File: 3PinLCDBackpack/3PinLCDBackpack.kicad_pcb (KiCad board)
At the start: 2 copper layers, 46.4 x 15.2 mm, 7 parts, among them J1 2-pin_power_input_header, J2 3-pin_LCD_header, Q1 BC547, U1 74HC595, U2 LCD_HD44780

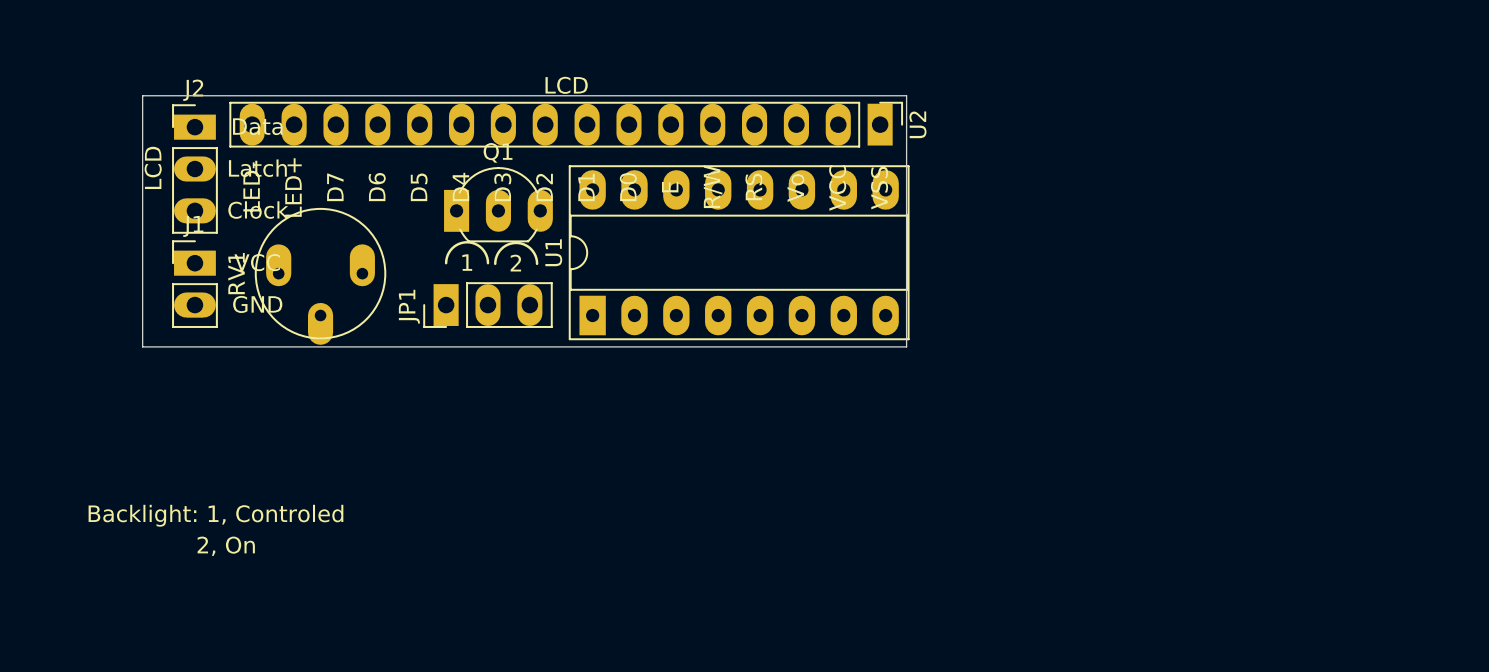
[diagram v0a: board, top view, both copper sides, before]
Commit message: 3 pin lcd backpack, new pcb
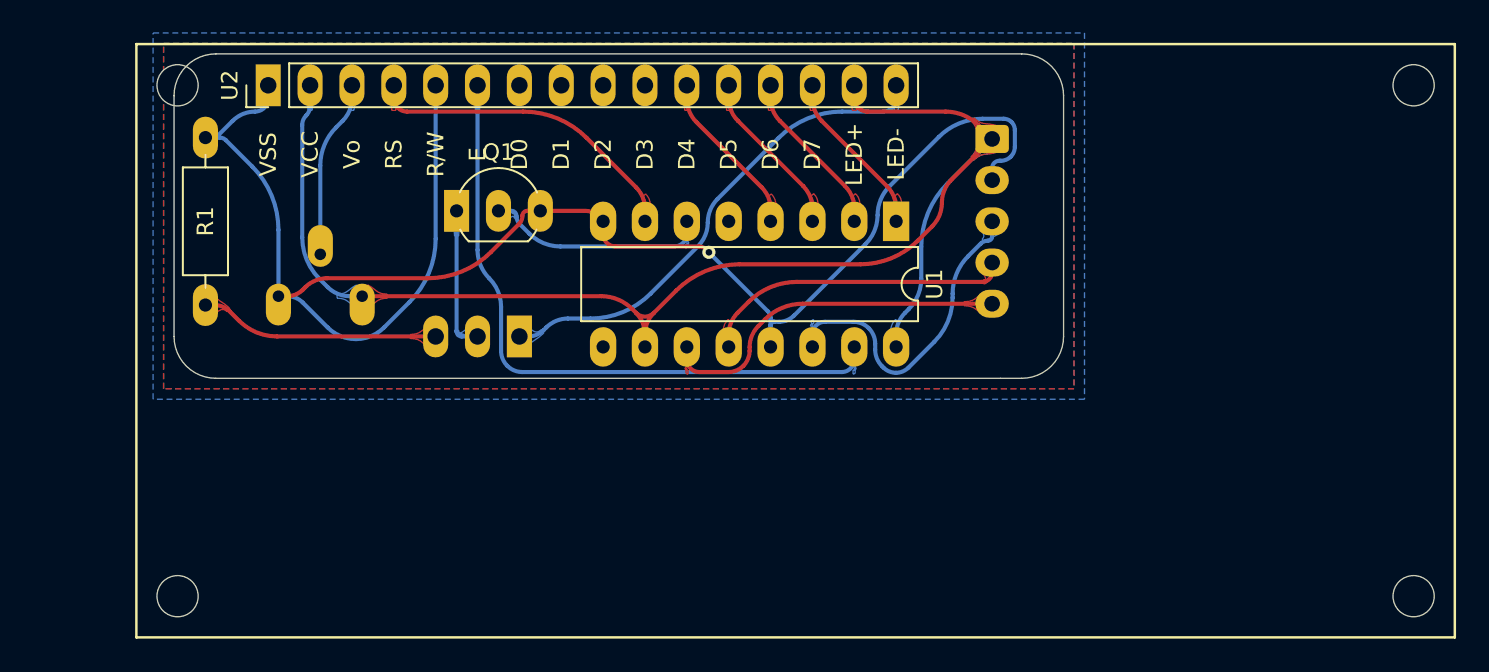
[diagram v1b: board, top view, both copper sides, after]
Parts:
- removed J1: 2-pin_power_input_header, My_Headers:2-pin_power_input_header_larger_pads
- removed J2: 3-pin_LCD_header, My_Headers:3-pin_LCD_header_larger_pads
- added R1: 56R, My_Misc:R_Axial_DIN0207_L6.3mm_D2.5mm_P10.16mm_Horizontal_larger_pads, F.Cu at (133.3, 57.1)
- added U3: 5-pin_LiquidCrystal595_connector, My_Headers:5-pin JST LiquidCrystal595, B.Cu at (181.1, 57.2)
- JP1, RV1: moved to B.Cu
- U1: footprint Package_DIP:DIP-16_W7.62mm_Socket_LongPads -> My_Misc:DIP-16_W7.62mm_LongPads w socket
- U2: footprint My_Headers:16-pin_LCD_header_larger_pads -> My_Parts:LCD_HD44780_16x2_w_headers_large
- moved U2 36.9 mm to (137.2, 54.0), turned to 0 degrees
- moved U1 19.3 mm to (175.3, 62.2), turned to -90 degrees
- moved JP1 4.84 mm to (152.4, 69.2)
- moved RV1 1.37 mm to (142.9, 66.8), turned to -90 degrees
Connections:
- JP1 pad 3: /GND -> Net-(JP1-Pad3)
- Q1 pad 3: /GND -> GND
- RV1 pad 1: /GND -> VCC
- RV1 pad 3: Net-(J1-Pad1) -> GND
- U1 pad 10: Net-(J1-Pad1) -> VCC
- U1 pad 13: /GND -> GND
- U1 pad 16: Net-(J1-Pad1) -> VCC
- U1 pad 5: Net-(U1-Pad5) -> unconnected-(U1-Pad5)
- U1 pad 8: /GND -> GND
- U1 pad 9: Net-(U1-Pad9) -> unconnected-(U1-Pad9)
- U2 pad 1: /GND -> GND
- U2 pad 10: Net-(U2-Pad10) -> unconnected-(U2-Pad10)
- U2 pad 15: Net-(J1-Pad1) -> VCC
- U2 pad 2: Net-(J1-Pad1) -> VCC
- U2 pad 5: /GND -> GND
- U2 pad 7: Net-(U2-Pad7) -> unconnected-(U2-Pad7)
- U2 pad 8: Net-(U2-Pad8) -> unconnected-(U2-Pad8)
- U2 pad 9: Net-(U2-Pad9) -> unconnected-(U2-Pad9)
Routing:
- net GND: track 0.00 -> 101.9 mm, vias 0 -> 1
- net VCC: track 0.00 -> 86.1 mm
- net Net-(U1-Pad15): track 0.00 -> 39.8 mm
- net Net-(JP1-Pad1): track 0.00 -> 29.9 mm
- net Net-(U1-Pad11): track 0.00 -> 21.9 mm
- net Net-(U1-Pad14): track 0.00 -> 19.8 mm
- net Net-(U1-Pad7): track 0.00 -> 19.8 mm
- net Net-(U1-Pad12): track 0.00 -> 19.1 mm
- net Net-(JP1-Pad3): track 0.00 -> 14.5 mm
- net Net-(Q1-Pad2): track 0.00 -> 13.5 mm
- net Net-(RV1-Pad2): track 0.00 -> 10.8 mm
- net Net-(U1-Pad3): track 0.00 -> 10.2 mm
- net Net-(U1-Pad2): track 0.00 -> 10.2 mm
- net Net-(U1-Pad1): track 0.00 -> 10.2 mm
- net Net-(U1-Pad4): track 0.00 -> 10.2 mm
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- added copper zone on B.Cu, net (none)
- added copper zone on B.Cu, net GND
- added copper zone on F.Cu, net GND
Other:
- board size 46.4 x 15.2 mm -> 54 x 19.7 mm
- net class Default removed
- board text added: "3PinLCDBackpack Design: Jon Sagebrand github.com/jonsag/miscPCBs"
- board text added: "JP1: 1-2 -> Controlled backlight 2-3 -> Backlight always on"
- board text removed: "1"
- board text removed: "2"
- board text removed: "2, On"
- board text removed: "3PinLCDBackPack-1.0 Design: Jon Sagebrand jonsagebrand@gmail.com github.com/jonsag"
- board text removed: "Backlight: 1, Controled"

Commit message: 3-pin
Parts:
- U2: footprint My_Parts:LCD_HD44780_16x2_w_headers_large -> My_Parts:LCD_HD44780_16x2_w_headers_no outlinelarge
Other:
- board text added: "1"
- board text added: "2"
- board text added: "3"
- board text added: "Clock"
- board text added: "Connector on other side"
- board text added: "Contrast"
- board text added: "Data"
- board text added: "GND"
- board text added: "JP1"
- board text added: "Latch"
- board text added: "Pot. on other side"
- board text added: "This side towards LCD"
- board text added: "VCC"

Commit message: 3pinLCD
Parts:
- JP1: footprint My_Parts:Jumper_1x03_P2.54mm_large -> My_Parts:Angled_Jumper_1x03_P2.54mm_large; moved to F.Cu
- moved JP1 1.91 mm to (152.4, 67.3), turned to -90 degrees
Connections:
- JP1 pad 1: Net-(JP1-Pad1) -> Net-(Q1-Pad1)
- JP1 pad 2: Net-(JP1-Pad2) -> Net-(U2-Pad16)
- Q1 pad 1: Net-(JP1-Pad2) -> Net-(Q1-Pad1)
- U2 pad 16: Net-(JP1-Pad1) -> Net-(U2-Pad16)
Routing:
- net Net-(U2-Pad16): track 0.00 -> 46.8 mm
- net Net-(JP1-Pad1): track 29.9 -> 0.00 mm
- net GND: track 101.9 -> 80.0 mm, vias 1 -> 0
- net Net-(JP1-Pad2): track 8.75 -> 0.00 mm
- net Net-(Q1-Pad1): track 0.00 -> 7.86 mm
- net VCC: track 86.1 -> 79.2 mm
- net Net-(U1-Pad15): track 39.8 -> 46.5 mm
- net Net-(U1-Pad14): track 19.8 -> 14.7 mm
- net Net-(U1-Pad12): track 19.1 -> 22.4 mm
- net Net-(U1-Pad11): track 21.9 -> 20.3 mm
- added copper zone on F.Cu, net (none)
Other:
- board text removed: "1"
- board text removed: "2"
- board text removed: "3"
- board text removed: "JP1"

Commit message: new pcb for 3pinlcd
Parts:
- added R2: 1k, My_Misc:R_Axial_DIN0207_L6.3mm_D2.5mm_P10.16mm_Horizontal_larger_pads, F.Cu at (136.5, 61.0)
- moved Q1 1.27 mm to (149.9, 61.6)
- moved U1 0.64 mm to (175.9, 62.2)
- moved RV1 0.63 mm to (142.9, 67.4)
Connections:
- U1 pad 6: Net-(Q1-Pad2) -> Net-(R2-Pad1)
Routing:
- net Net-(R2-Pad1): track 0.00 -> 28.6 mm
- net Net-(JP1-Pad2): track 46.8 -> 32.6 mm
- net Net-(U1-Pad15): track 46.5 -> 33.7 mm
- net GND: track 80.0 -> 86.5 mm
- net Net-(Q1-Pad2): track 13.3 -> 7.11 mm
- net Net-(U1-Pad14): track 14.7 -> 17.7 mm
- net VCC: track 79.2 -> 81.3 mm
- net Net-(JP1-Pad1): track 7.86 -> 7.03 mm
- net Net-(U1-Pad12): track 22.4 -> 21.7 mm
- net Net-(RV1-Pad2): track 10.8 -> 11.4 mm
- net Net-(U1-Pad11): track 20.3 -> 19.7 mm
- net Net-(U1-Pad4): track 10.2 -> 10.7 mm
- net Net-(U1-Pad3): track 10.2 -> 10.7 mm
- net Net-(U1-Pad2): track 10.2 -> 10.7 mm
- net Net-(U1-Pad1): track 10.2 -> 10.7 mm
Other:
- board text added: "1"
- board text added: "2"
- board text added: "3"
- board text added: "JP1"
- board text added: "JP1: 1<->2: Controlled backlight -> R1 = 1k, Q1 = BC547 2<->3: Backlight always on -> R2 = 56R"
- board text added: "Shift Register, 74HC595"
- board text removed: "JP1: 1-2 -> Controlled backlight 2-3 -> Backlight always on"
